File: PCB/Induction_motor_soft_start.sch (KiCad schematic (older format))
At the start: 26 parts, among them J1 Conn_01x12, J2 Conn_01x12, SW1 Manual triggering, U1 SFH620A-3, U2 EL817

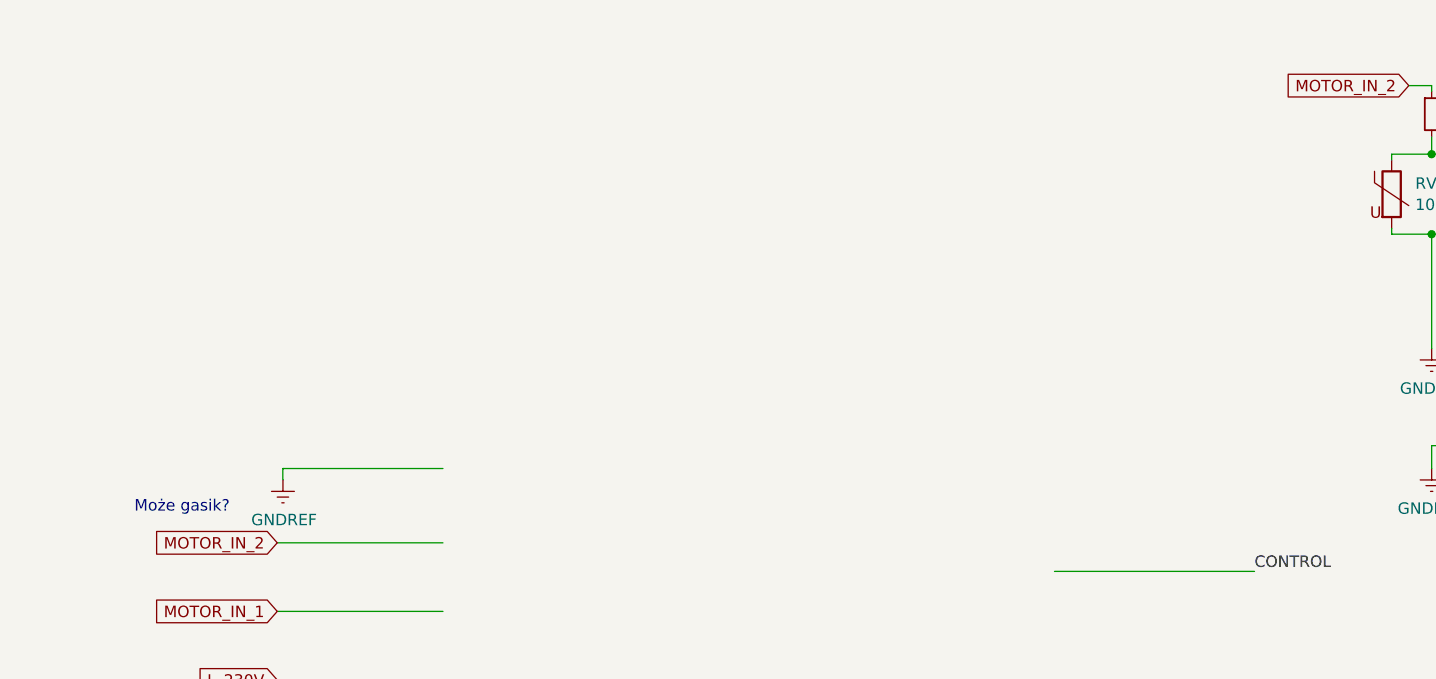
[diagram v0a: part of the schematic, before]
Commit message: Add info about triac
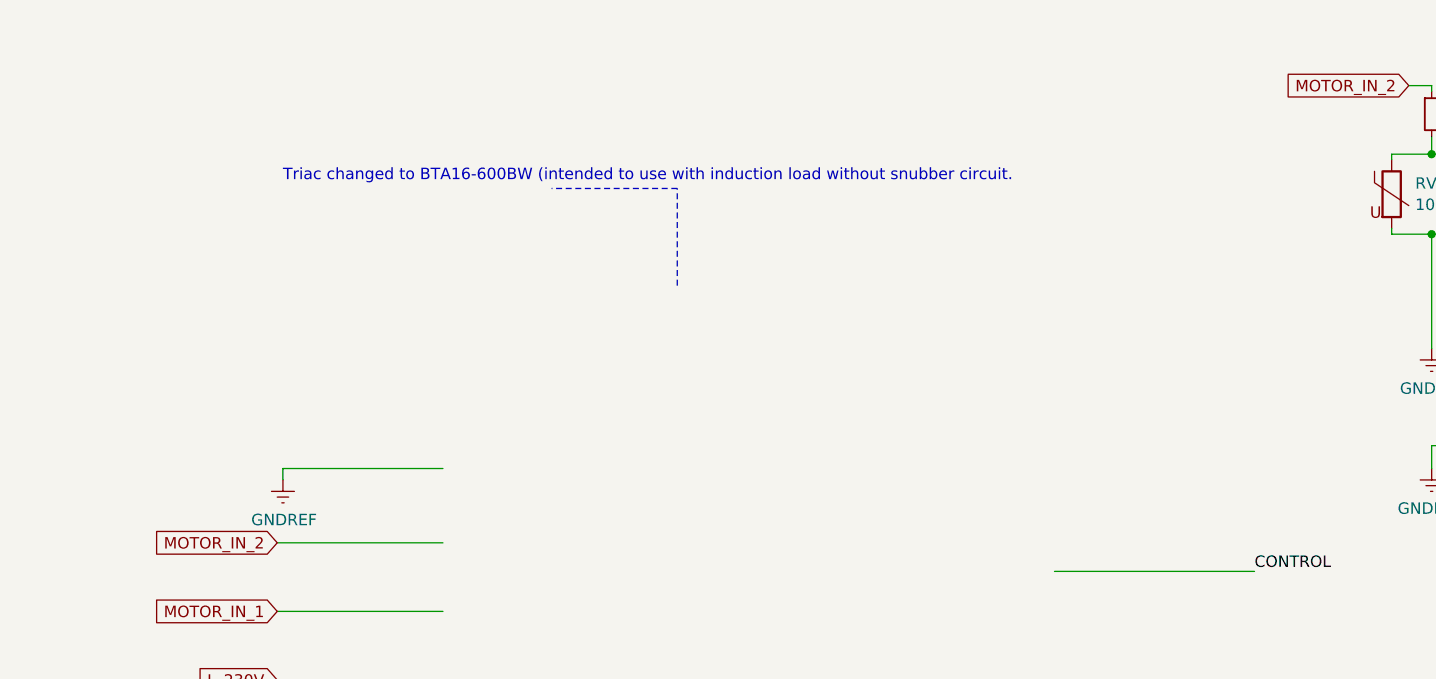
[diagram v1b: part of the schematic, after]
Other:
- note added: "Triac changed to BTA16-600BW (intended to use with induction load without snubber circuit."
- note removed: "Może gasik?"
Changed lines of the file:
@@
 Text Notes 8325 5400 0    50   ~ 0
 CONTROL IN \nPWM ~100Hz\nOC0A
-Text Notes 1250 5400 0    50   ~ 0
-Może gasik?
 $Bitmap
 Pos 4100 5650
@@
 Text Label 2350 1725 3    50   ~ 0
 PA5_(User_LED)
+Wire Notes Line
+	3625 4400 3625 3975
+Wire Notes Line
+	3625 3975 3075 3975
+Text Notes 1900 3950 0    50   ~ 0
+Triac changed to BTA16-600BW (intended to use with induction load without snubber circuit.
 $EndSCHEMATC
